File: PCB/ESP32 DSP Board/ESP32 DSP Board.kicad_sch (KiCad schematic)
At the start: 89 parts, among them J1 USB4216-03-A_REVA, SW1 PTS810_SJM_250_SMTR_LFS, SW2 PTS810_SJM_250_SMTR_LFS, U8 ESP32-S3-WROOM-1, U9 TPS73733DCQ

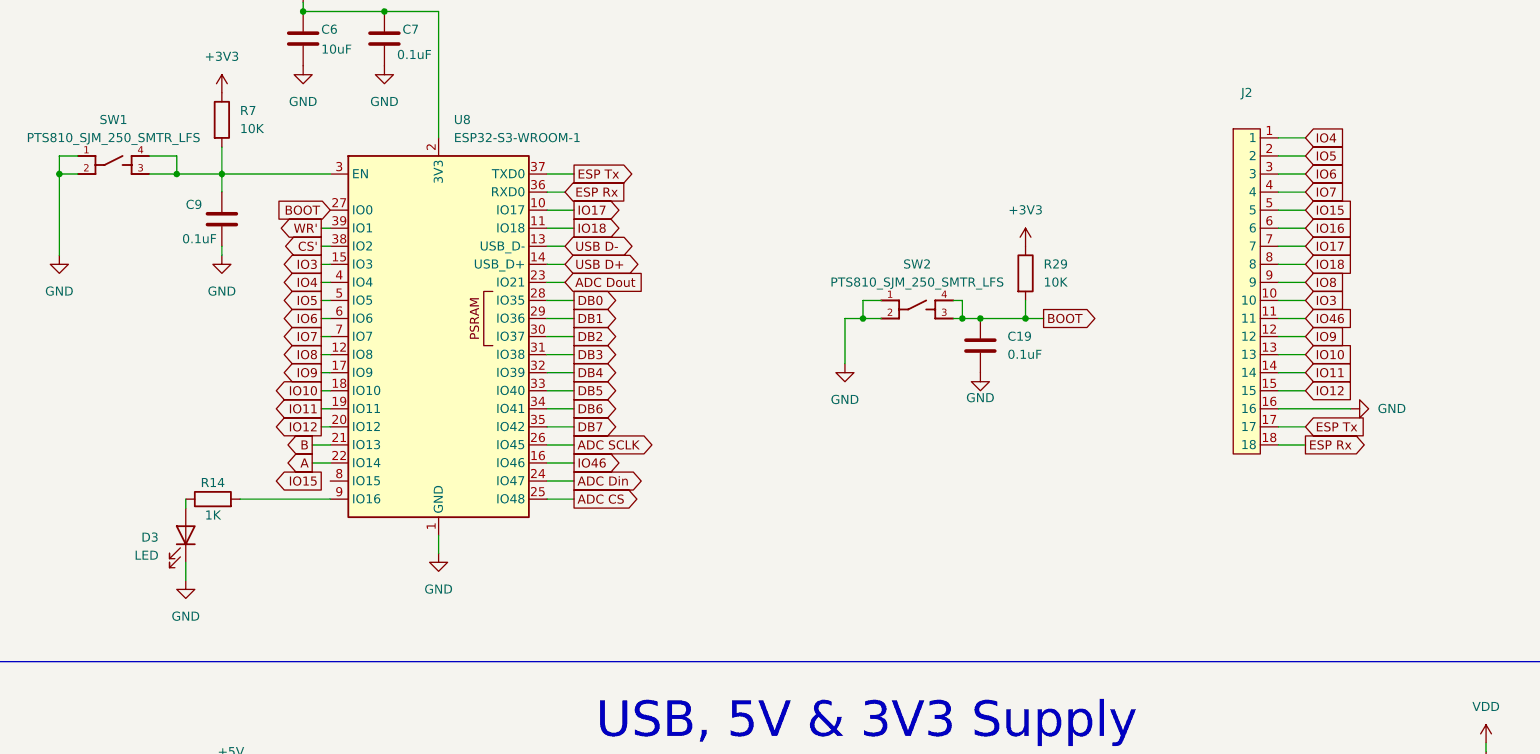
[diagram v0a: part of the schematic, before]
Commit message: Layer stackup changed to 6 layers, DAC routing started
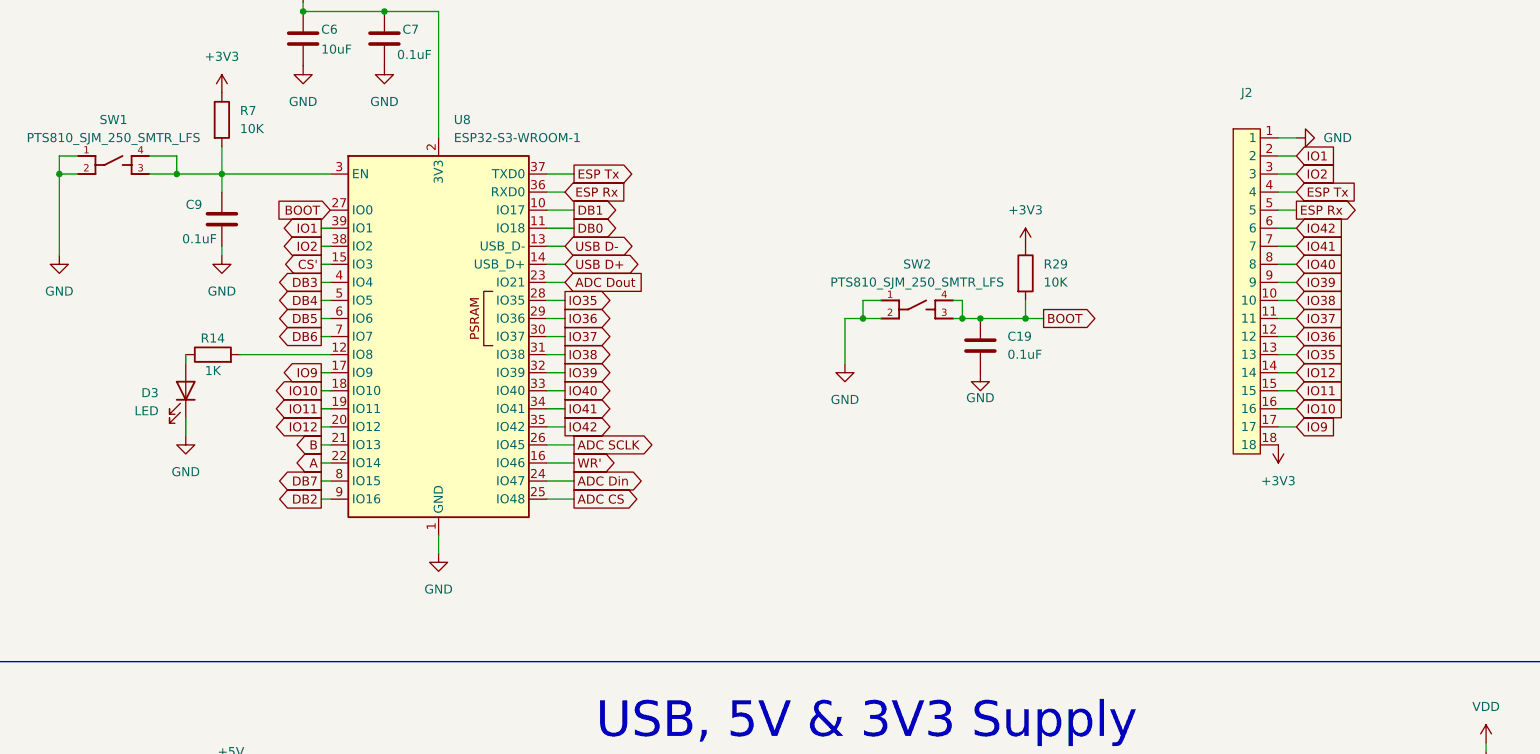
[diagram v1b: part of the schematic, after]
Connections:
- net IO15 is gone; now on net ESP Rx: J2.5
- net +3V3: now also J2.18
- net CS': now also U8.15 (IO3); no longer U8.38 (IO2)
- net DB0: now also U8.11 (IO18); no longer U8.28 (IO35)
- net DB1: now also U8.10 (IO17); no longer U8.29 (IO36)
- net DB2: now also U8.9 (IO16); no longer U8.30 (IO37)
- net DB3: now also U8.4 (IO4); no longer U8.31 (IO38)
- net DB4: now also U8.5 (IO5); no longer U8.32 (IO39)
- net DB5: now also U8.6 (IO6); no longer U8.33 (IO40)
- net DB6: now also U8.7 (IO7); no longer U8.34 (IO41)
- net DB7: now also U8.8 (IO15); no longer U8.35 (IO42)
- net ESP Rx: no longer J2.18
- net ESP Tx: now also J2.4; no longer J2.17
- net GND: now also J2.1; no longer J2.16
- net IO10: now also J2.16; no longer J2.13
- net IO11: now also J2.15; no longer J2.14
- net IO12: now also J2.14; no longer J2.15
- net IO9: now also J2.17; no longer J2.12
- net WR': now also U8.16 (IO46); no longer U8.39 (IO1)
- net at R14.2: now also U8.12 (IO8); no longer U8.9 (IO16)
- net IO16 renamed IO42
- net IO42: now also U8.35 (IO42)
- net IO17 renamed IO41
- net IO41: now also U8.34 (IO41); no longer U8.10 (IO17)
- net IO18 renamed IO40
- net IO40: now also U8.33 (IO40); no longer U8.11 (IO18)
- net IO3 renamed IO38
- net IO38: now also U8.31 (IO38); no longer U8.15 (IO3)
- removed net IO4: J2.1, U8.4 (IO4)
- net IO46 renamed IO37
- net IO37: now also U8.30 (IO37); no longer U8.16 (IO46)
- net IO5 renamed IO1
- net IO1: now also U8.39 (IO1); no longer U8.5 (IO5)
- net IO6 renamed IO2
- net IO2: now also U8.38 (IO2); no longer U8.6 (IO6)
- removed net IO7: J2.4, U8.7 (IO7)
- net IO8 renamed IO39
- net IO39: now also U8.32 (IO39); no longer U8.12 (IO8)
- new net IO35: J2.13, U8.28 (IO35)
- new net IO36: J2.12, U8.29 (IO36)
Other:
- moved on the sheet: D3, R14

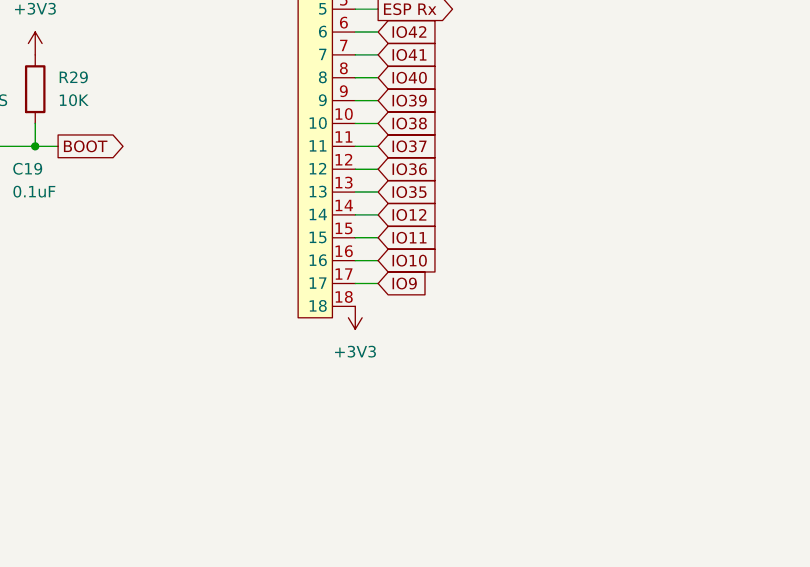
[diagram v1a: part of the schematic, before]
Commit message: Digital layout changed, pins moved closer to mcu, routing completed before checks
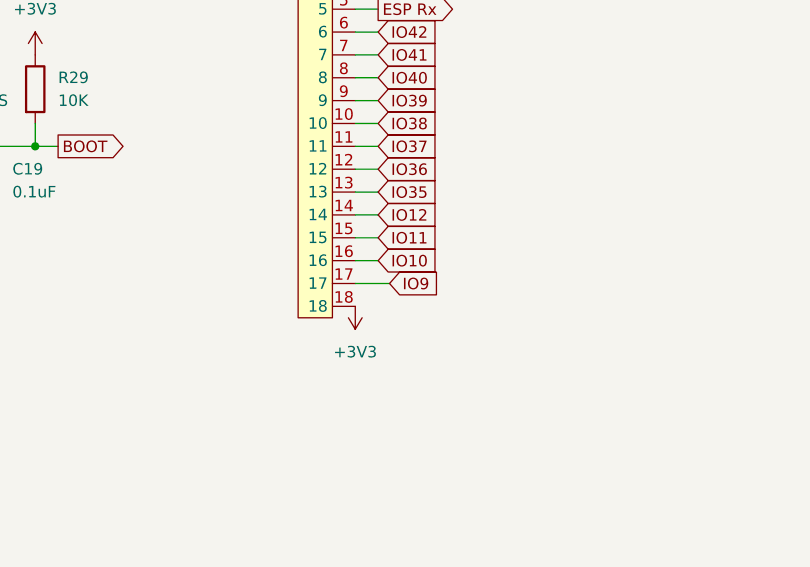
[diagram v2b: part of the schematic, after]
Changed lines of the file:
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@@
 	(wire
 		(pts
+			(xy 341.63 152.4) (xy 344.17 152.4)
+		)
+		(stroke
+			(width 0)
+			(type default)
+		)
+	)
+	(wire
+		(pts
 			(xy 306.07 139.7) (xy 308.61 139.7)
 		)
@@
 	(wire
 		(pts
+			(xy 341.63 147.32) (xy 344.17 147.32)
+		)
+		(stroke
+			(width 0)
+			(type default)
+		)
+	)
+	(wire
+		(pts
 			(xy 250.19 55.88) (xy 278.13 55.88)
 		)
@@
 	(wire
 		(pts
+			(xy 341.63 149.86) (xy 344.17 149.86)
+		)
+		(stroke
+			(width 0)
+			(type default)
+		)
+	)
+	(wire
+		(pts
 			(xy 241.3 121.92) (xy 238.76 121.92)
 		)
@@
 	(wire
 		(pts
-			(xy 341.63 149.86) (xy 344.17 149.86)
-		)
-		(stroke
-			(width 0)
-			(type default)
-		)
-	)
-	(wire
-		(pts
 			(xy 238.76 147.32) (xy 241.3 147.32)
 		)
@@
 	(wire
 		(pts
-			(xy 341.63 154.94) (xy 344.17 154.94)
-		)
-		(stroke
-			(width 0)
-			(type default)
-		)
-	)
-	(wire
-		(pts
 			(xy 341.63 134.62) (xy 344.17 134.62)
 		)
@@
 	(wire
 		(pts
+			(xy 341.63 154.94) (xy 345.44 154.94)
+		)
+		(stroke
+			(width 0)
+			(type default)
+		)
+	)
+	(wire
+		(pts
 			(xy 242.57 157.48) (xy 238.76 157.48)
 		)
@@
 	(wire
 		(pts
-			(xy 341.63 147.32) (xy 344.17 147.32)
-		)
-		(stroke
-			(width 0)
-			(type default)
-		)
-	)
-	(wire
-		(pts
 			(xy 242.57 215.9) (xy 245.11 215.9)
 		)
@@
 	(wire
 		(pts
-			(xy 341.63 152.4) (xy 344.17 152.4)
-		)
-		(stroke
-			(width 0)
-			(type default)
-		)
-	)
-	(wire
-		(pts
 			(xy 82.55 215.9) (xy 87.63 215.9)
 		)
@@
 	(global_label "IO9"
 		(shape input)
-		(at 344.17 154.94 0)
+		(at 345.44 154.94 0)
 		(fields_autoplaced yes)
 		(effects
@@
 		)
 		(property "Intersheetrefs" "${INTERSHEET_REFS}"
-			(at 350.3 154.94 0)
+			(at 351.57 154.94 0)
 			(effects
 				(font
@@
 		(on_board yes)
 		(dnp no)
-		(fields_autoplaced yes)
 		(property "Reference" "#PWR086"
 			(at 341.63 153.67 0)

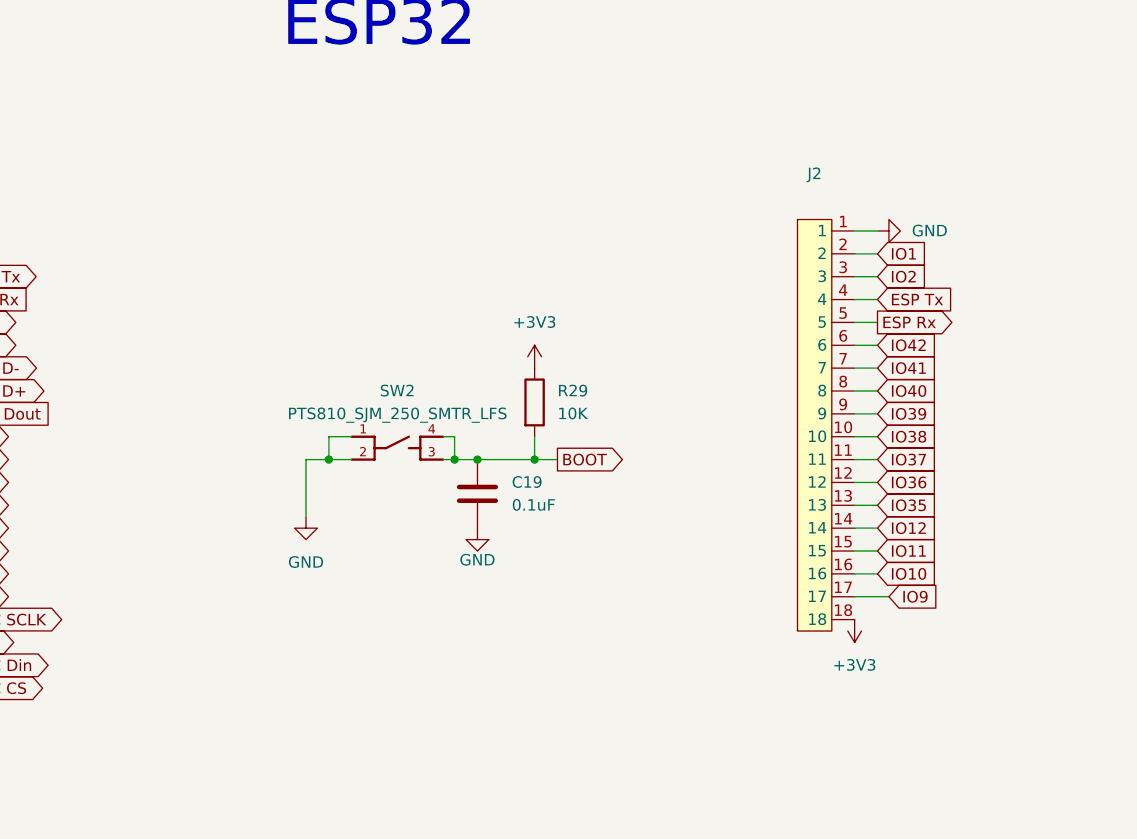
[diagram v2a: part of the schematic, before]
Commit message: Silkscreen added to connectors
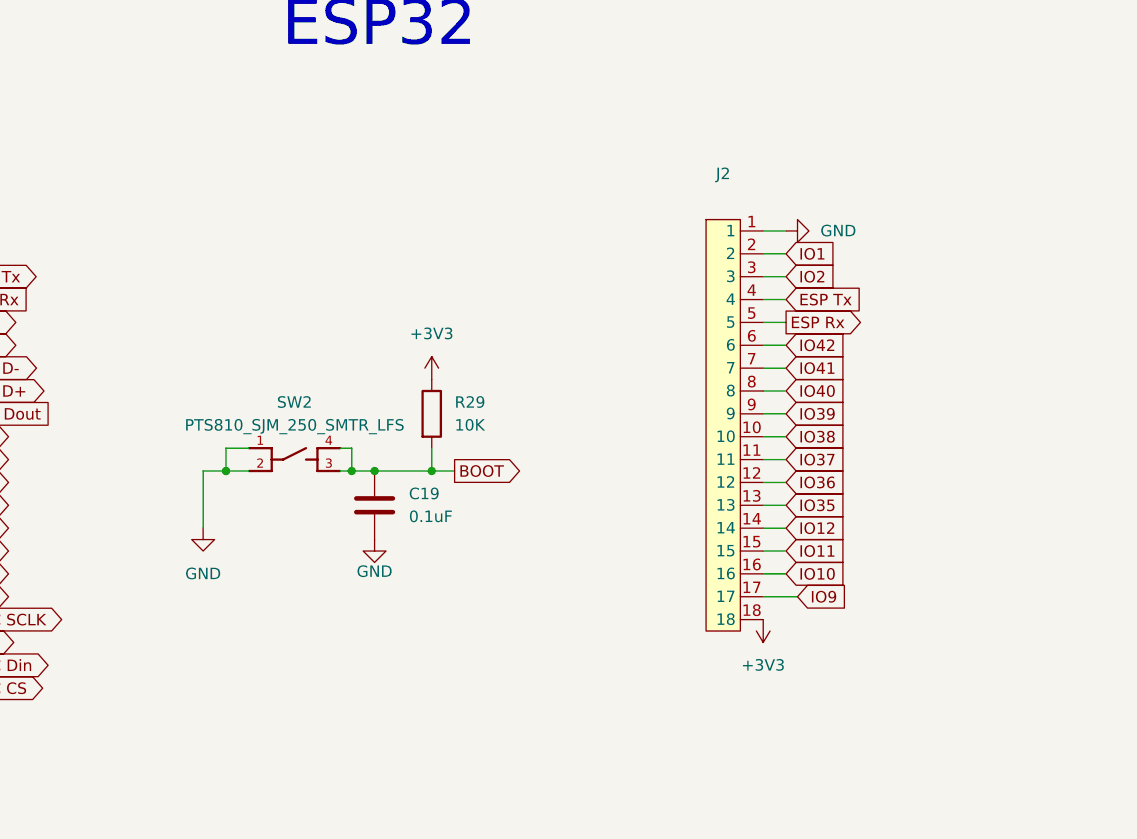
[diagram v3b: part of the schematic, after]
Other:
- moved on the sheet: C19, J2, R29, SW2

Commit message: Input filter altered, output amplifier fixed, 22uf decoupling added to charge pump negative output
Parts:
- removed C20, C21: 100p, Capacitor_SMD:C_01005_0402Metric, symbol Device:C
- removed C23: 0.1uF, Capacitor_SMD:C_0402_1005Metric, symbol Device:C
- removed C28: 10nF, Capacitor_SMD:C_0402_1005Metric, symbol Device:C
- removed D10, D5, D6, D7, D8, D9: D_Zener, Diode_SMD:D_SOD-123, symbol Device:D_Zener
- removed R12, R13: 10K, Resistor_SMD:R_0402_1005Metric, symbol Device:R
- removed R15: 1K, Resistor_SMD:R_0402_1005Metric, symbol Device:R
- removed R16: 23.2K, Resistor_SMD:R_0402_1005Metric, symbol Device:R
- removed R17, R18, R30, R31: 2K, Resistor_SMD:R_0402_1005Metric, symbol Device:R
- removed R32: 95.3K, Resistor_SMD:R_0402_1005Metric, symbol Device:R
- removed U4: ~, Package_DIP:DIP-8_W7.62mm, symbol Amplifier_Operational_TI:TL072CP
- removed U5: ~, LDO_Adjustable:TPS73601DBVT, symbol LDO_TI:TPS736
- added U11: ~, symbol Amplifier_Operational_TI:OPA4227PA
- C1: value 10uF -> 0.1uF; footprint Capacitor_SMD:C_0603_1608Metric -> Capacitor_SMD:C_0402_1005Metric
- C10: value 0.1uF -> C; footprint Capacitor_SMD:C_0402_1005Metric -> (none)
- C11, C2: value 10uF -> C; footprint Capacitor_SMD:C_0603_1608Metric -> (none)
- C15: value 10uF -> 22uF
- C17, C18: value 100p -> C; footprint Capacitor_SMD:C_01005_0402Metric -> (none)
- C8: value 1uF -> C; footprint Capacitor_SMD:C_0603_1608Metric -> (none)
- J1: footprint USB_Connector:GCT_USB4216-03-A_REVA -> USB4216-03-A_REVA:GCT_USB4216-03-A_REVA
- R1, R10, R11, R2, R8, R9: value 10K -> R; footprint Resistor_SMD:R_0402_1005Metric -> (none)
- R19, R21: value 10K -> 5.1K
- R22: value 15K -> 11K
- R23: value 22K -> 20K
- SW1, SW2: footprint Switches:SW_PTS810_SJM_250_SMTR_LFS -> PTS810_SJM_250_SMTR_LFS:SW_PTS810_SJM_250_SMTR_LFS
- U9: footprint LDO_3V3:TPS73733DCQ -> TPS73733DCQ:SOT127P706X180-6N
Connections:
- net +3.3V is gone; now on net +3V3: J7.2, R6.1
- net CH1 IN is gone; now on net CH1_FOUT: U2.2 (CH1)
- net +3V3: now also U1.1 (OUT1)
- net +5V: now also C1.1, U11.4 (V+); no longer C10.2
- net -5V: now also U11.11 (V-)
- net 2B: now also R25.2, U7.7 (2OUT); no longer R24.1, R25.1, U7.6 (2IN-)
- net ADC CH0: now also R1.2
- net ADC CH1: now also R9.2
- net ADC CH2: no longer U2.3 (CH2)
- net ADC CH3: no longer U2.4 (CH3)
- net CH0_FOUT: now also C8.1, U2.1 (CH0), U11.13 (-InD), U11.14 (OutD); no longer C18.2, R1.1
- net CH1_FOUT: now also C17.2, U11.8 (OutC), U11.9 (-InC); no longer R10.1
- net GND: now also C1.2, C10.2, C18.2, C2.2; no longer C10.1, C17.2, R11.2, R2.2, U1.1 (OUT1)
- net at J5.1: now also R20.1, R21.1, R22.1, R23.1, U12.6 (OUT); no longer C8.1
- net at C17.1: now also R10.1, R11.2
- net at C18.1: now also R11.1, U11.10 (+InC)
- net 1.5V: no longer names the net of C11.1
- net 1.5V: now also R10.2, R9.1; no longer R8.2
- removed net CH0 IN: R9.2, U2.1 (CH0)
- new net: R24.1, R25.1, U7.6 (2IN-)
- new net: C10.1, R8.1, U11.12 (+InD)
- new net: C2.1, R1.1, R2.2
- new net: C8.2, R2.1, R8.2
- new net CH2_FOUT: U2.3 (CH2)
- new net CH3_FOUT: U2.4 (CH3)
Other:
- moved on the sheet: C19, C26, C6, C7, C9, D3, J2, J5, R14, R24, R25, R26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

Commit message: Footprints changed to 1206 for resistors and capacitors, PCB restarted
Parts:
- added C20, C21, C23, C28, C29, C30: 47p, Capacitor_SMD:C_1206_3216Metric_Pad1.33x1.80mm_HandSolder, symbol Device:C
- added R12, R13, R15, R16, R17, R18: 33K, Resistor_SMD:R_1206_3216Metric_Pad1.30x1.75mm_HandSolder, symbol Device:R
- C1, C12, C22, C24, C25, C26, C27: footprint Capacitor_SMD:C_0402_1005Metric -> Capacitor_SMD:C_1206_3216Metric_Pad1.33x1.80mm_HandSolder
- C10, C11, C17, C18, C2, C8: value C -> 47p; footprint (none) -> Capacitor_SMD:C_1206_3216Metric_Pad1.33x1.80mm_HandSolder
- C13, C14, C19, C7, C9: footprint Capacitor_SMD:C_01005_0402Metric -> Capacitor_SMD:C_1206_3216Metric_Pad1.33x1.80mm_HandSolder
- C15: footprint Capacitor_SMD:C_0603_1608Metric -> Capacitor_THT:CP_Radial_Tantal_D4.5mm_P2.50mm
- C16, C3, C4, C5: footprint Capacitor_SMD:C_0603_1608Metric -> Capacitor_SMD:C_1206_3216Metric_Pad1.33x1.80mm_HandSolder
- C6: footprint Capacitor_SMD:C_0805_2012Metric -> Capacitor_SMD:C_1206_3216Metric_Pad1.33x1.80mm_HandSolder
- R1, R10, R11, R2, R8, R9: value R -> 33K; footprint (none) -> Resistor_SMD:R_1206_3216Metric_Pad1.30x1.75mm_HandSolder
- R14, R19, R20, R21, R22, R23, R24, R25, R26, R27, R29, R3, R4, R5, R6, R7: footprint Resistor_SMD:R_0402_1005Metric -> Resistor_SMD:R_1206_3216Metric_Pad1.30x1.75mm_HandSolder
- R28: footprint Resistor_SMD:R_0805_2012Metric -> Resistor_SMD:R_1206_3216Metric_Pad1.30x1.75mm_HandSolder
- U11: footprint (none) -> Package_DIP:CERDIP-14_W7.62mm_SideBrazed
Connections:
- net ADC CH2: now also R12.1
- net ADC CH3: now also R16.1
- net CH2_FOUT: now also U11.6 (-InB), U11.7 (OutB), C21.2
- net CH3_FOUT: now also U11.1 (OutA), U11.2 (-InA), C29.1
- net GND: now also C20.2, C23.2, C28.1, C30.1
- net at U11.3 (+InA): now also C30.2, R18.2
- net at U11.5 (+InB): now also C23.1, R15.2
- new net: C21.1, R13.2, R15.1
- new net: C20.1, R12.2, R13.1
- new net: C29.2, R17.2, R18.1
- new net: C28.2, R16.2, R17.1
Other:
- moved on the sheet: C1, C10, C11, C17, C18, C2, C27, C3, C4, C5, C6, C7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

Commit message: latest commit before laptop migration
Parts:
- D1, D2, D4: footprint LED_SMD:LED_0805_2012Metric -> LED_SMD:LED_1206_3216Metric_Pad1.42x1.75mm_HandSolder
- D3: footprint LED_SMD:LED_0603_1608Metric -> LED_SMD:LED_1206_3216Metric_Pad1.42x1.75mm_HandSolder
- J1: footprint USB4216-03-A_REVA:GCT_USB4216-03-A_REVA -> USB_Connector:GCT_USB4216-03-A_REVA
- SW1, SW2: footprint PTS810_SJM_250_SMTR_LFS:SW_PTS810_SJM_250_SMTR_LFS -> Switches:SW_PTS810_SJM_250_SMTR_LFS
- U9: footprint TPS73733DCQ:SOT127P706X180-6N -> LDO_3V3:TPS73733DCQ
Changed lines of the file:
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@@
 	(polyline
 		(pts
-			(xy 215.9 81.28) (xy 215.9 187.96)
+			(xy 215.9 83.82) (xy 215.9 187.96)
 		)
 		(stroke
@@
 			)
 		)
-		(property "Footprint" "TPS73733DCQ:SOT127P706X180-6N"
+		(property "Footprint" "LDO_3V3:TPS73733DCQ"
 			(at 213.36 238.76 0)
 			(effects
@@
 			)
 		)
-		(property "Footprint" "PTS810_SJM_250_SMTR_LFS:SW_PTS810_SJM_250_SMTR_LFS"
+		(property "Footprint" "Switches:SW_PTS810_SJM_250_SMTR_LFS"
 			(at 322.58 130.81 0)
 			(effects
@@
 			)
 		)
-		(property "Footprint" "LED_SMD:LED_0805_2012Metric"
+		(property "Footprint" "LED_SMD:LED_1206_3216Metric_Pad1.42x1.75mm_HandSolder"
 			(at 300.99 224.79 0)
 			(effects
@@
 			)
 		)
-		(property "Footprint" "LED_SMD:LED_0603_1608Metric"
+		(property "Footprint" "LED_SMD:LED_1206_3216Metric_Pad1.42x1.75mm_HandSolder"
 			(at 240.03 151.13 0)
 			(effects
@@
 			)
 		)
-		(property "Footprint" "LED_SMD:LED_0805_2012Metric"
+		(property "Footprint" "LED_SMD:LED_1206_3216Metric_Pad1.42x1.75mm_HandSolder"
 			(at 325.12 224.79 0)
 			(effects
@@
 			)
 		)
-		(property "Footprint" "PTS810_SJM_250_SMTR_LFS:SW_PTS810_SJM_250_SMTR_LFS"
+		(property "Footprint" "Switches:SW_PTS810_SJM_250_SMTR_LFS"
 			(at 229.87 118.11 0)
 			(effects
@@
 			)
 		)
-		(property "Footprint" "LED_SMD:LED_0805_2012Metric"
+		(property "Footprint" "LED_SMD:LED_1206_3216Metric_Pad1.42x1.75mm_HandSolder"
 			(at 312.42 224.79 0)
 			(effects
@@
 			)
 		)
-		(property "Footprint" "USB4216-03-A_REVA:GCT_USB4216-03-A_REVA"
+		(property "Footprint" "USB_Connector:GCT_USB4216-03-A_REVA"
 			(at 140.97 229.87 0)
 			(effects
